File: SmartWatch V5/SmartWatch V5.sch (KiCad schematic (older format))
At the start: 57 parts, among them J1 10118192-0001LF, J10 TestPad, J2 , J8 TestPad, J9 TestPad, Q1 FDN340P, Q2 MMBT3904, Q3 MMBT3904, Q4 FDN028N20, Q5 FDN028N20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

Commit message: PCB Routing for REV5
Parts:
- removed R4: 0 (NC), Resistor_SMD:R_0603_1608Metric, symbol Device:R
- removed R5: 0, Resistor_SMD:R_0603_1608Metric, symbol Device:R
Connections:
- net LDO_EN is gone; now on net BAT+: U3.4 (EN)
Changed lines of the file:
@@
 	-1   0    0    -1
 $EndComp
-Text Label 2750 1000 0    50   ~ 0
-BAT_ALRT
-$Comp
-L Device:R R5
-U 1 1 5EA97DC3
-P 3300 1000
-F 0 "R5" H 3370 1046 50  0000 L CNN
-F 1 "0" H 3370 955 50  0000 L CNN
-F 2 "Resistor_SMD:R_0603_1608Metric" V 3230 1000 50  0001 C CNN
-F 3 "~" H 3300 1000 50  0001 C CNN
-F 4 "311-0.0GRCT-ND" H 3300 1000 50  0001 C CNN "digikey"
-	1    3300 1000
-	0    1    1    0
-$EndComp
-Wire Wire Line
-	2750 1000 3150 1000
-$Comp
-L Device:R R4
-U 1 1 5EAB0896
-P 3300 850
-F 0 "R4" H 3150 900 50  0000 L CNN
-F 1 "0 (NC)" H 3000 800 50  0000 L CNN
-F 2 "Resistor_SMD:R_0603_1608Metric" V 3230 850 50  0001 C CNN
-F 3 "~" H 3300 850 50  0001 C CNN
-F 4 "311-0.0GRCT-ND" H 3300 850 50  0001 C CNN "digikey"
-	1    3300 850
-	0    1    1    0
-$EndComp
-Wire Wire Line
-	2900 850  3150 850
 Text Notes 600  650  0    50   ~ 0
 Battery And Power Management
@@
 	1    0    0    -1
 $EndComp
-Wire Wire Line
-	3550 1000 3550 850
-Wire Wire Line
-	3450 1000 3550 1000
-Wire Wire Line
-	3450 850  3550 850
-Wire Wire Line
-	3550 850  3850 850
-Connection ~ 3550 850
 Text Label 3850 850  2    50   ~ 0
 LDO_EN
@@
 Wire Wire Line
 	7950 2550 8400 2550
+Wire Wire Line
+	2900 850  3850 850
 $EndSCHEMATC

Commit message: Completed Rev 5 Board Layout and Routing
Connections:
- net BAT+: no longer U3.4 (EN)
- net PWR_IN: now also U3.4 (EN)
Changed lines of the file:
@@
 	1    0    0    -1
 $EndComp
-Text Label 3850 850  2    50   ~ 0
-LDO_EN
-Wire Wire Line
-	3650 1400 4050 1400
-Text Label 3650 1400 0    50   ~ 0
-LDO_EN
 Wire Wire Line
 	4400 1750 4400 1700
@@
 Wire Bus Line
 	550  4700 550  7600
-Text Label 2900 850  0    50   ~ 0
-BAT+
 Wire Wire Line
 	8400 2450 7950 2450
@@
 BAT_SENSE
 Wire Wire Line
-	3200 1300 4050 1300
+	3200 1300 3550 1300
 $Comp
 L CustomParts:ZJY117 A1
@@
 	7950 2550 8400 2550
 Wire Wire Line
-	2900 850  3850 850
+	3550 1300 3550 1400
+Wire Wire Line
+	3550 1400 4050 1400
+Connection ~ 3550 1300
+Wire Wire Line
+	3550 1300 4050 1300
 $EndSCHEMATC

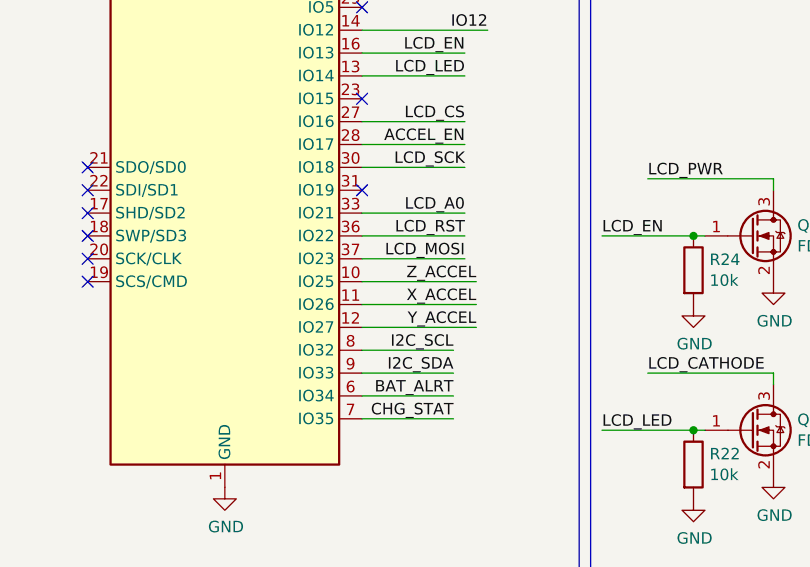
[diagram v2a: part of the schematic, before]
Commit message: Completed New Layout and Routing of Rev 5 (overall improved)
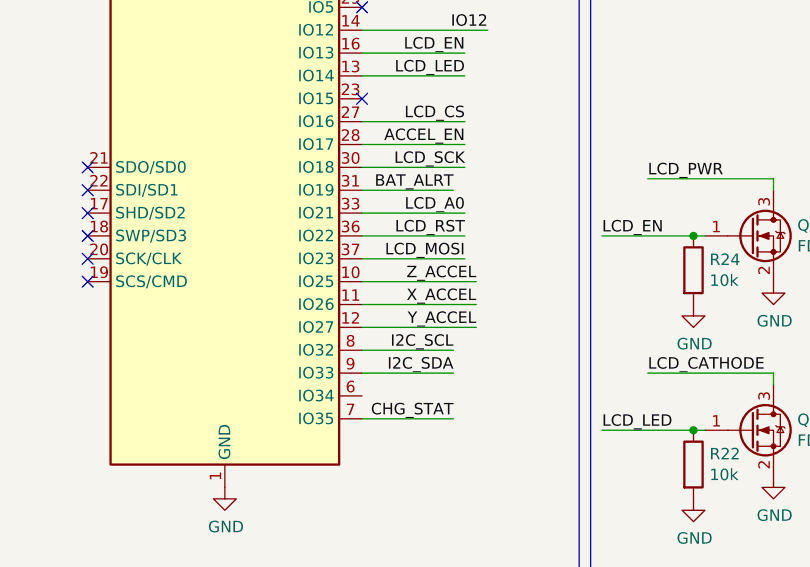
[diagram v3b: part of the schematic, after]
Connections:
- net BAT_ALRT: now also U6.31 (IO19); no longer U6.6 (IO34)
- no-connect marks 28 -> 27
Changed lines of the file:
@@
 $EndDescr
-$Comp
-L RF_Module:ESP32-WROOM-32 U6
-U 1 1 5E6BFC95
-P 7350 2650
-F 0 "U6" H 6600 4250 50  0000 C CNN
-F 1 "ESP32-WROOM-32" H 6900 4150 50  0000 C CNN
-F 2 "RF_Module:ESP32-WROOM-32" H 7350 1150 50  0001 C CNN
-F 3 "https://www.espressif.com/sites/default/files/documentation/esp32-wroom-32_datasheet_en.pdf" H 7050 2700 50  0001 C CNN
-F 4 "1904-1010-1-ND" H 7350 2650 50  0001 C CNN "digikey"
-	1    7350 2650
-	1    0    0    -1
-$EndComp
 $Comp
 L power:+3.3V #PWR0101
@@
 Text Label 8350 3750 2    50   ~ 0
 CHG_STAT
-Text Label 8350 3650 2    50   ~ 0
-BAT_ALRT
-Wire Wire Line
-	7950 3650 8350 3650
+Wire Wire Line
+	7950 2750 8350 2750
 Wire Wire Line
 	7950 3750 8350 3750
@@
 NoConn ~ 4050 6800
 NoConn ~ 7950 1950
-NoConn ~ 7950 2750
 $Comp
 L Device:Thermistor TH1
@@
 Wire Wire Line
 	3550 1300 4050 1300
+$Comp
+L RF_Module:ESP32-WROOM-32 U6
+U 1 1 5E6BFC95
+P 7350 2650
+F 0 "U6" H 6600 4250 50  0000 C CNN
+F 1 "ESP32-WROOM-32" H 6900 4150 50  0000 C CNN
+F 2 "RF_Module:ESP32-WROOM-32" H 7350 1150 50  0001 C CNN
+F 3 "https://www.espressif.com/sites/default/files/documentation/esp32-wroom-32_datasheet_en.pdf" H 7050 2700 50  0001 C CNN
+F 4 "1904-1010-1-ND" H 7350 2650 50  0001 C CNN "digikey"
+	1    7350 2650
+	1    0    0    -1
+$EndComp
+Text Label 8350 2750 2    50   ~ 0
+BAT_ALRT
 $EndSCHEMATC

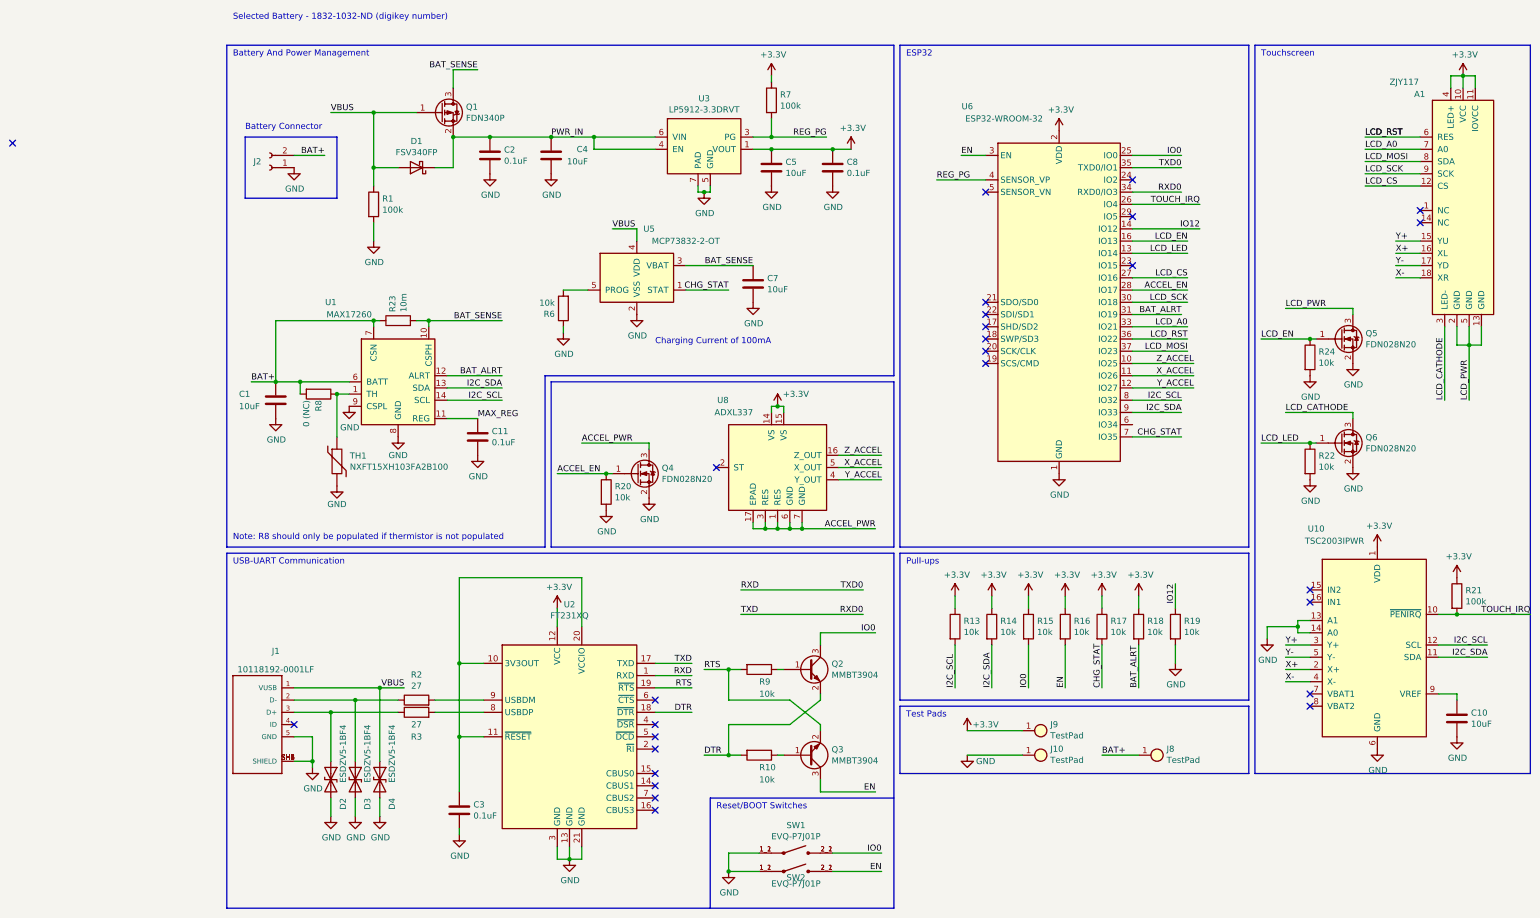
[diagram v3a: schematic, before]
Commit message: Added additional capacitence where board space permits
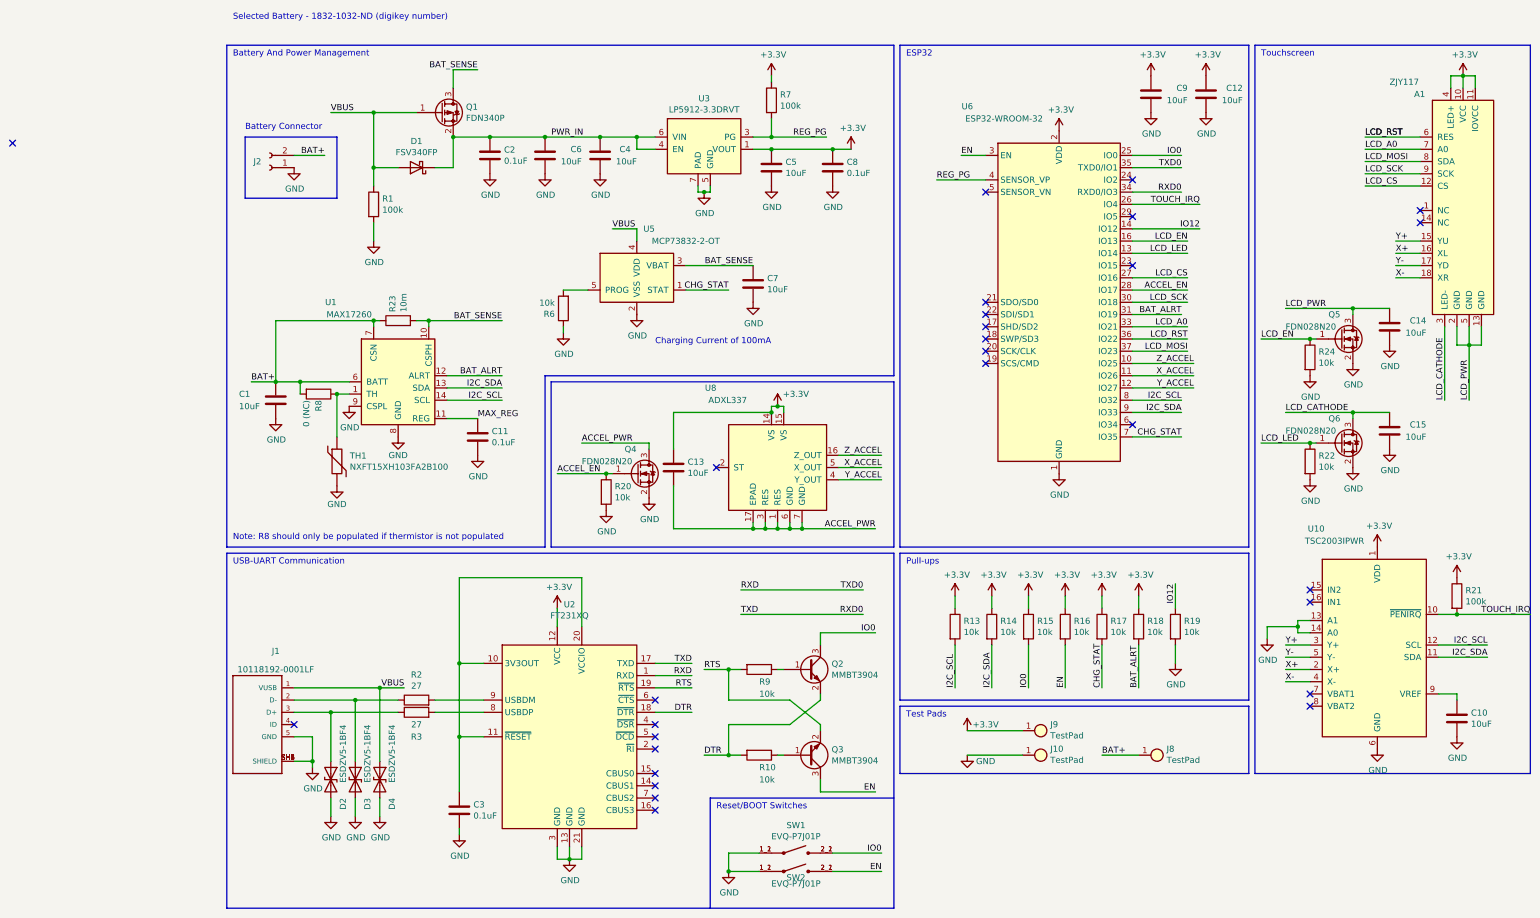
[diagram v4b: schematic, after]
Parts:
- added C12, C13, C14, C15, C6, C9: 10uF, Capacitor_SMD:C_0603_1608Metric, symbol Device:C
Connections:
- net +3V3: now also C12.1, C13.1, C9.1
- net ACCEL_PWR: now also C13.2
- net GND: now also C12.2, C14.2, C15.2, C6.2, C9.2
- net LCD_CATHODE: now also C15.1
- net LCD_PWR: now also C14.1
- net PWR_IN: now also C6.1
- no-connect marks 27 -> 28
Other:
- moved on the sheet: C4
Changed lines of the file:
@@
 L power:GND #PWR0121
 U 1 1 5E85A156
-P 3200 1600
-F 0 "#PWR0121" H 3200 1350 50  0001 C CNN
-F 1 "GND" H 3205 1427 50  0000 C CNN
-F 2 "" H 3200 1600 50  0001 C CNN
-F 3 "" H 3200 1600 50  0001 C CNN
-	1    3200 1600
+P 3600 1600
+F 0 "#PWR0121" H 3600 1350 50  0001 C CNN
+F 1 "GND" H 3605 1427 50  0000 C CNN
+F 2 "" H 3600 1600 50  0001 C CNN
+F 3 "" H 3600 1600 50  0001 C CNN
+	1    3600 1600
 	1    0    0    -1
 $EndComp
@@
 L Device:C C4
 U 1 1 5E927609
-P 3200 1450
-F 0 "C4" H 2900 1500 50  0000 L CNN
-F 1 "10uF" H 2900 1400 50  0000 L CNN
-F 2 "Capacitor_SMD:C_0603_1608Metric" H 3238 1300 50  0001 C CNN
-F 3 "~" H 3200 1450 50  0001 C CNN
-F 4 "478-10766-1-ND" H 3200 1450 50  0001 C CNN "digikey"
-	1    3200 1450
+P 3600 1450
+F 0 "C4" H 3350 1500 50  0000 L CNN
+F 1 "10uF" H 3300 1400 50  0000 L CNN
+F 2 "Capacitor_SMD:C_0603_1608Metric" H 3638 1300 50  0001 C CNN
+F 3 "~" H 3600 1450 50  0001 C CNN
+F 4 "478-10766-1-ND" H 3600 1450 50  0001 C CNN "digikey"
+	1    3600 1450
 	-1   0    0    -1
 $EndComp
@@
 	2400 1300 2700 1300
 Connection ~ 2400 1300
-Connection ~ 3200 1300
-Connection ~ 2700 1300
-Wire Wire Line
-	2700 1300 3200 1300
 Wire Wire Line
 	2250 1550 2400 1550
@@
 	0    -1   -1   0
 $EndComp
-Text Label 3200 1300 0    50   ~ 0
-PWR_IN
 $Comp
 L CustomParts:10118192-0001LF J1
@@
 U 1 1 5F663623
 P 5050 4000
-F 0 "U8" H 4650 4550 50  0000 R CNN
-F 1 "ADXL337" H 4850 4450 50  0000 R CNN
+F 0 "U8" H 4550 4650 50  0000 R CNN
+F 1 "ADXL337" H 4800 4550 50  0000 R CNN
 F 2 "CustomFootprints:ADXL337BCPZ-RL" H 4600 4450 50  0001 C CNN
 F 3 "https://www.analog.com/media/en/technical-documentation/data-sheets/ADXL337.pdf" H 4600 4450 50  0001 C CNN
@@
 Text Label 4850 2350 2    50   ~ 0
 BAT_SENSE
-Wire Wire Line
-	3200 1300 3550 1300
 $Comp
 L CustomParts:ZJY117 A1
@@
 U 1 1 5F89B605
 P 9650 3800
-F 0 "Q6" H 9854 3846 50  0000 L CNN
-F 1 "FDN028N20" H 9854 3755 50  0000 L CNN
+F 0 "Q6" H 9550 4000 50  0000 L CNN
+F 1 "FDN028N20" H 9200 3900 50  0000 L CNN
 F 2 "Package_TO_SOT_SMD:SOT-23" H 9850 3900 50  0001 C CNN
 F 3 "https://www.onsemi.com/pub/Collateral/FDN028N20-D.pdf" H 9650 3800 50  0001 C CNN
@@
 U 1 1 5F89CF73
 P 9650 2950
-F 0 "Q5" H 9854 2996 50  0000 L CNN
-F 1 "FDN028N20" H 9854 2905 50  0000 L CNN
+F 0 "Q5" H 9550 3150 50  0000 L CNN
+F 1 "FDN028N20" H 9200 3050 50  0000 L CNN
 F 2 "Package_TO_SOT_SMD:SOT-23" H 9850 3050 50  0001 C CNN
 F 3 "https://www.onsemi.com/pub/Collateral/FDN028N20-D.pdf" H 9650 2950 50  0001 C CNN
@@
 U 1 1 5F89D454
 P 3900 4050
-F 0 "Q4" H 4104 4096 50  0000 L CNN
-F 1 "FDN028N20" H 4104 4005 50  0000 L CNN
+F 0 "Q4" H 3800 4250 50  0000 L CNN
+F 1 "FDN028N20" H 3450 4150 50  0000 L CNN
 F 2 "Package_TO_SOT_SMD:SOT-23" H 4100 4150 50  0001 C CNN
 F 3 "https://www.onsemi.com/pub/Collateral/FDN028N20-D.pdf" H 3900 4050 50  0001 C CNN
@@
 Wire Wire Line
 	7950 2550 8400 2550
-Wire Wire Line
-	3550 1300 3550 1400
-Wire Wire Line
-	3550 1400 4050 1400
-Connection ~ 3550 1300
-Wire Wire Line
-	3550 1300 4050 1300
 $Comp
 L RF_Module:ESP32-WROOM-32 U6
@@
 Text Label 8350 2750 2    50   ~ 0
 BAT_ALRT
+NoConn ~ 7950 3650
+$Comp
+L power:+3.3V #PWR0129
+U 1 1 5F52C376
+P 8550 800
+F 0 "#PWR0129" H 8550 650 50  0001 C CNN
+F 1 "+3.3V" H 8565 973 50  0000 C CNN
+F 2 "" H 8550 800 50  0001 C CNN
+F 3 "" H 8550 800 50  0001 C CNN
+	1    8550 800
+	1    0    0    -1
+$EndComp
+$Comp
+L power:+3.3V #PWR0130
+U 1 1 5F52BED2
+P 8100 800
+F 0 "#PWR0130" H 8100 650 50  0001 C CNN
+F 1 "+3.3V" H 8115 973 50  0000 C CNN
+F 2 "" H 8100 800 50  0001 C CNN
+F 3 "" H 8100 800 50  0001 C CNN
+	1    8100 800
+	1    0    0    -1
+$EndComp
+$Comp
+L Device:C C12
+U 1 1 5F50D6DD
+P 8550 950
+F 0 "C12" H 8250 1000 50  0000 L CNN
+F 1 "10uF" H 8250 900 50  0000 L CNN
+F 2 "Capacitor_SMD:C_0603_1608Metric" H 8588 800 50  0001 C CNN
+F 3 "~" H 8550 950 50  0001 C CNN
+F 4 "478-10766-1-ND" H 8550 950 50  0001 C CNN "digikey"
+	1    8550 950
+	-1   0    0    -1
+$EndComp
+$Comp
+L power:GND #PWR0132
+U 1 1 5F50D6D6
+P 8550 1100
+F 0 "#PWR0132" H 8550 850 50  0001 C CNN
+F 1 "GND" H 8555 927 50  0000 C CNN
+F 2 "" H 8550 1100 50  0001 C CNN
+F 3 "" H 8550 1100 50  0001 C CNN
+	1    8550 1100
+	1    0    0    -1
+$EndComp
+$Comp
+L Device:C C9
+U 1 1 5F4FF12B
+P 8100 950
+F 0 "C9" H 7800 1000 50  0000 L CNN
+F 1 "10uF" H 7800 900 50  0000 L CNN
+F 2 "Capacitor_SMD:C_0603_1608Metric" H 8138 800 50  0001 C CNN
+F 3 "~" H 8100 950 50  0001 C CNN
+F 4 "478-10766-1-ND" H 8100 950 50  0001 C CNN "digikey"
+	1    8100 950
+	-1   0    0    -1
+$EndComp
+$Comp
+L power:GND #PWR0144
+U 1 1 5F4FF124
+P 8100 1100
+F 0 "#PWR0144" H 8100 850 50  0001 C CNN
+F 1 "GND" H 8105 927 50  0000 C CNN
+F 2 "" H 8100 1100 50  0001 C CNN
+F 3 "" H 8100 1100 50  0001 C CNN
+	1    8100 1100
+	1    0    0    -1
+$EndComp
+$Comp
+L Device:C C6
+U 1 1 5F4F0B7A
+P 3150 1450
+F 0 "C6" H 2850 1500 50  0000 L CNN
+F 1 "10uF" H 2850 1400 50  0000 L CNN
+F 2 "Capacitor_SMD:C_0603_1608Metric" H 3188 1300 50  0001 C CNN
+F 3 "~" H 3150 1450 50  0001 C CNN
+F 4 "478-10766-1-ND" H 3150 1450 50  0001 C CNN "digikey"
+	1    3150 1450
+	-1   0    0    -1
+$EndComp
+$Comp
+L power:GND #PWR0148
+U 1 1 5F4F0B73
+P 3150 1600
+F 0 "#PWR0148" H 3150 1350 50  0001 C CNN
+F 1 "GND" H 3155 1427 50  0000 C CNN
+F 2 "" H 3150 1600 50  0001 C CNN
+F 3 "" H 3150 1600 50  0001 C CNN
+	1    3150 1600
+	1    0    0    -1
+$EndComp
+$Comp
+L Device:C C13
+U 1 1 5F57BD73
+P 4200 4000
+F 0 "C13" H 4315 4046 50  0000 L CNN
+F 1 "10uF" H 4315 3955 50  0000 L CNN
+F 2 "Capacitor_SMD:C_0603_1608Metric" H 4238 3850 50  0001 C CNN
+F 3 "~" H 4200 4000 50  0001 C CNN
+F 4 "478-10766-1-ND" H 4200 4000 50  0001 C CNN "digikey"
+	1    4200 4000
+	1    0    0    -1
+$EndComp
+Wire Wire Line
+	5000 3550 4200 3550
+Wire Wire Line
+	4200 3550 4200 3850
+Connection ~ 5000 3550
+Wire Wire Line
+	4200 4150 4200 4500
+Wire Wire Line
+	4200 4500 4850 4500
+Connection ~ 4850 4500
+$Comp
+L Device:C C15
+U 1 1 5F5E65A4
+P 10050 3700
+F 0 "C15" H 9750 3750 50  0000 L CNN
+F 1 "10uF" H 9750 3650 50  0000 L CNN
+F 2 "Capacitor_SMD:C_0603_1608Metric" H 10088 3550 50  0001 C CNN
+F 3 "~" H 10050 3700 50  0001 C CNN
+F 4 "478-10766-1-ND" H 10050 3700 50  0001 C CNN "digikey"
+	1    10050 3700
+	-1   0    0    -1
+$EndComp
+$Comp
+L Device:C C14
+U 1 1 5F5E8029
+P 10050 2850
+F 0 "C14" H 9750 2900 50  0000 L CNN
+F 1 "10uF" H 9750 2800 50  0000 L CNN
+F 2 "Capacitor_SMD:C_0603_1608Metric" H 10088 2700 50  0001 C CNN
+F 3 "~" H 10050 2850 50  0001 C CNN
+F 4 "478-10766-1-ND" H 10050 2850 50  0001 C CNN "digikey"
+	1    10050 2850
+	-1   0    0    -1
+$EndComp
+Wire Wire Line
+	9750 2700 10050 2700
+Connection ~ 9750 2700
+Wire Wire Line
+	9750 3550 10050 3550
+Connection ~ 9750 3550
+$Comp
+L power:GND #PWR0149
+U 1 1 5F60734E
+P 10050 3850
+F 0 "#PWR0149" H 10050 3600 50  0001 C CNN
+F 1 "GND" H 10055 3677 50  0000 C CNN
+F 2 "" H 10050 3850 50  0001 C CNN
+F 3 "" H 10050 3850 50  0001 C CNN
+	1    10050 3850
+	1    0    0    -1
+$EndComp
+$Comp
+L power:GND #PWR0150
+U 1 1 5F6077C7
+P 10050 3000
+F 0 "#PWR0150" H 10050 2750 50  0001 C CNN
+F 1 "GND" H 10055 2827 50  0000 C CNN
+F 2 "" H 10050 3000 50  0001 C CNN
+F 3 "" H 10050 3000 50  0001 C CNN
+	1    10050 3000
+	1    0    0    -1
+$EndComp
+Wire Wire Line
+	3900 1300 3900 1400
+Wire Wire Line
+	3900 1400 4050 1400
+Connection ~ 3900 1300
+Wire Wire Line
+	3900 1300 4050 1300
+Connection ~ 2700 1300
+Text Label 3200 1300 0    50   ~ 0
+PWR_IN
+Connection ~ 3600 1300
+Wire Wire Line
+	3600 1300 3900 1300
+Wire Wire Line
+	2700 1300 3150 1300
+Connection ~ 3150 1300
+Wire Wire Line
+	3150 1300 3600 1300
 $EndSCHEMATC

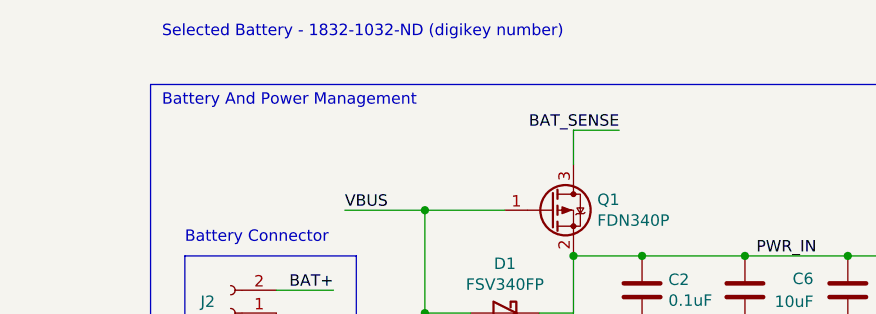
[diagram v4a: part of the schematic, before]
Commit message: Switched Selected Battery
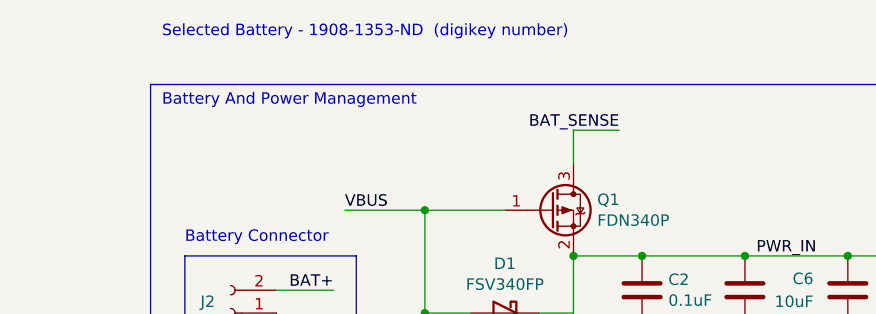
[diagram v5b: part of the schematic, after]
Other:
- note added: "Selected Battery - 1908-1353-ND (digikey number)"
- note removed: "Selected Battery - 1832-1032-ND (digikey number)"
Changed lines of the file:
@@
 NoConn ~ -1200 1350
 Text Notes 600  350  0    50   ~ 0
-Selected Battery - 1832-1032-ND (digikey number)
+Selected Battery - 1908-1353-ND  (digikey number)
 Wire Wire Line
 	4750 5000 5750 5000
